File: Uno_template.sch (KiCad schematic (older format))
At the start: 4 parts

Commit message: initial commit
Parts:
- J1, J4: renamed from J?; footprint (none) -> Pin_Headers:Pin_Header_Straight_1x08_Pitch2.54mm
- J2: renamed from J?; footprint (none) -> Pin_Headers:Pin_Header_Straight_1x06_Pitch2.54mm
- J3: renamed from J?; footprint (none) -> Pin_Headers:Pin_Header_Straight_1x10_Pitch2.54mm
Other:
- note added: "Heizungssteuerung"
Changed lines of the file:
@@
 LIBS:contrib
 LIBS:valves
+LIBS:Uno_template-cache
 EELAYER 25 0
 EELAYER END
@@
 $EndDescr
 $Comp
-L Conn_01x08 J?
+L Conn_01x08 J1
 U 1 1 5A4D3F50
 P 7350 1250
-F 0 "J?" H 7350 1650 50  0000 C CNN
+F 0 "J1" H 7350 1650 50  0000 C CNN
 F 1 "POWER" H 7350 750 50  0000 C CNN
-F 2 "" H 7350 1250 50  0001 C CNN
+F 2 "Pin_Headers:Pin_Header_Straight_1x08_Pitch2.54mm" H 7350 1250 50  0001 C CNN
 F 3 "" H 7350 1250 50  0001 C CNN
 	1    7350 1250
@@
 1 = N.C.\n2 = IOREF\n3 = RESET\n4 = 3.3V\n5 = 5V\n6 = GND\n7 = GND\n8 = Vin
 $Comp
-L Conn_01x06 J?
+L Conn_01x06 J2
 U 1 1 5A4D408D
 P 7350 2350
-F 0 "J?" H 7350 2650 50  0000 C CNN
+F 0 "J2" H 7350 2650 50  0000 C CNN
 F 1 "ANALOG IN" H 7350 1950 50  0000 C CNN
-F 2 "" H 7350 2350 50  0001 C CNN
+F 2 "Pin_Headers:Pin_Header_Straight_1x06_Pitch2.54mm" H 7350 2350 50  0001 C CNN
 F 3 "" H 7350 2350 50  0001 C CNN
 	1    7350 2350
@@
 1 = A0\n2 = A1\n3 = A2\n4 = A3\n5 = A4\n6 = A5
 $Comp
-L Conn_01x08 J?
+L Conn_01x08 J4
 U 1 1 5A4D413D
 P 9850 2350
-F 0 "J?" H 9850 1850 50  0000 C CNN
+F 0 "J4" H 9850 1850 50  0000 C CNN
 F 1 "IOL" H 9850 2750 50  0000 C CNN
-F 2 "" H 9850 2350 50  0001 C CNN
+F 2 "Pin_Headers:Pin_Header_Straight_1x08_Pitch2.54mm" H 9850 2350 50  0001 C CNN
 F 3 "" H 9850 2350 50  0001 C CNN
 	1    9850 2350
@@
 $EndComp
 $Comp
-L Conn_01x10 J?
+L Conn_01x10 J3
 U 1 1 5A4D4192
 P 9850 1250
-F 0 "J?" H 9850 650 50  0000 C CNN
+F 0 "J3" H 9850 650 50  0000 C CNN
 F 1 "IOH" H 9850 1750 50  0000 C CNN
-F 2 "" H 9850 1250 50  0001 C CNN
+F 2 "Pin_Headers:Pin_Header_Straight_1x10_Pitch2.54mm" H 9850 1250 50  0001 C CNN
 F 3 "" H 9850 1250 50  0001 C CNN
 	1    9850 1250
@@
 Vin
 $Comp
-L +3V3 #PWR?
+L +3V3 #PWR01
 U 1 1 5A4D447E
 P 8300 1150
-F 0 "#PWR?" H 8300 1000 50  0001 C CNN
+F 0 "#PWR01" H 8300 1000 50  0001 C CNN
 F 1 "+3V3" H 8300 1290 50  0000 C CNN
 F 2 "" H 8300 1150 50  0001 C CNN
@@
 $EndComp
 $Comp
-L +5V #PWR?
+L +5V #PWR02
 U 1 1 5A4D449A
 P 8450 1250
-F 0 "#PWR?" H 8450 1100 50  0001 C CNN
+F 0 "#PWR02" H 8450 1100 50  0001 C CNN
 F 1 "+5V" H 8450 1390 50  0000 C CNN
 F 2 "" H 8450 1250 50  0001 C CNN
@@
 $EndComp
 $Comp
-L GND #PWR?
+L GND #PWR03
 U 1 1 5A4D44D1
 P 8300 1650
-F 0 "#PWR?" H 8300 1400 50  0001 C CNN
+F 0 "#PWR03" H 8300 1400 50  0001 C CNN
 F 1 "GND" H 8300 1500 50  0000 C CNN
 F 2 "" H 8300 1650 50  0001 C CNN
@@
 RX
 $Comp
-L GND #PWR?
+L GND #PWR04
 U 1 1 5A4D49BF
 P 8900 1150
-F 0 "#PWR?" H 8900 900 50  0001 C CNN
+F 0 "#PWR04" H 8900 900 50  0001 C CNN
 F 1 "GND" H 8900 1000 50  0000 C CNN
 F 2 "" H 8900 1150 50  0001 C CNN
@@
 Wire Wire Line
 	8900 1050 8900 1150
+Text Notes 7450 6950 0    197  ~ 0
+Heizungssteuerung
 $EndSCHEMATC

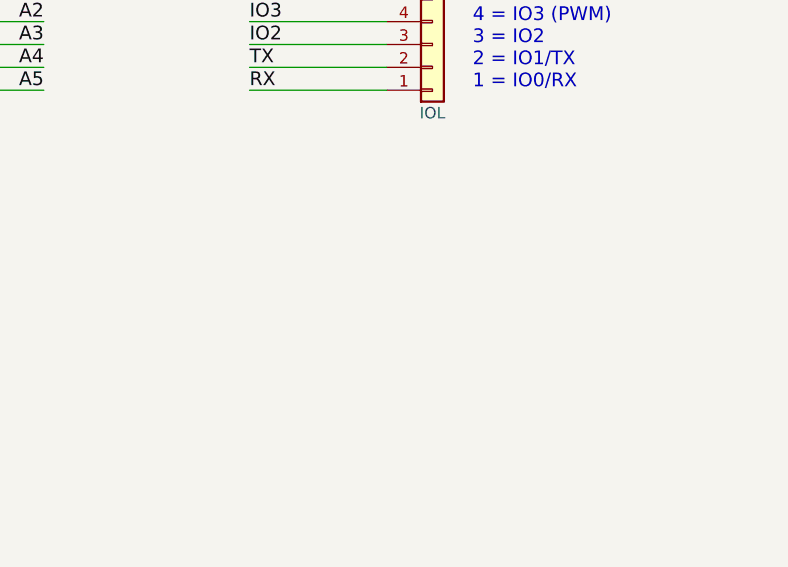
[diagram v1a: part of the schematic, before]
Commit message: Schaltplan: 1Wire interface added
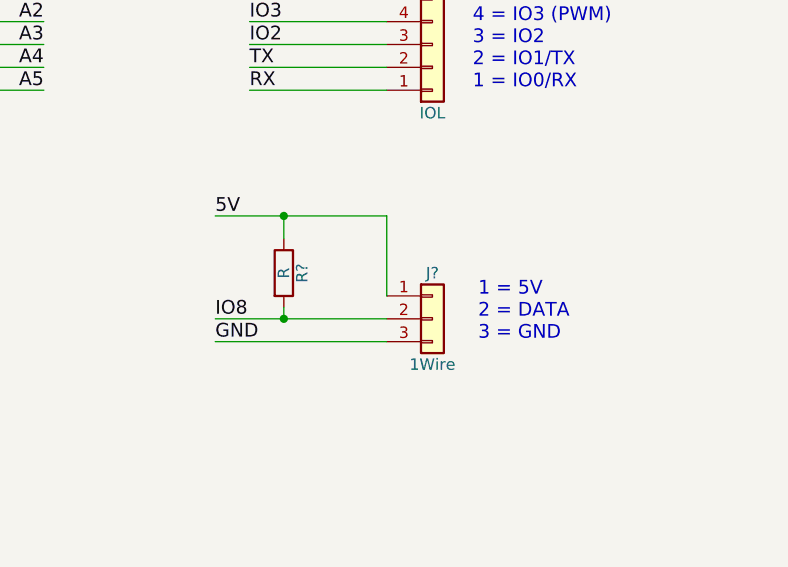
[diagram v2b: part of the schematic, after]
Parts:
- added J?: 1Wire, symbol Conn_01x03
- added R?: R, symbol R
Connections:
- net +5V: now also J?.1 (Pin_1), R?.1
- net GND: now also J?.3 (Pin_3)
- net IO8: now also J?.2 (Pin_2), R?.2
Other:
- note added: "1 = 5V\n2 = DATA\n3 = GND"
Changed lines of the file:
@@
 	1    0    0    -1
 $EndComp
-Wire Wire Line
-	7550 1050 8150 1050
-Wire Wire Line
-	7550 1150 8150 1150
-Wire Wire Line
-	7550 1250 8300 1250
-Wire Wire Line
-	7550 1350 8450 1350
-Wire Wire Line
-	7550 1450 8300 1450
-Wire Wire Line
-	7550 1550 8300 1550
-Wire Wire Line
-	7550 1650 8150 1650
-Wire Wire Line
-	8300 1250 8300 1150
-Wire Wire Line
-	8450 1350 8450 1250
-Wire Wire Line
-	8300 1450 8300 1650
-Connection ~ 8300 1550
-Wire Wire Line
-	7550 2150 8150 2150
-Wire Wire Line
-	7550 2250 8150 2250
-Wire Wire Line
-	7550 2350 8150 2350
-Wire Wire Line
-	7550 2450 8150 2450
-Wire Wire Line
-	7550 2550 8150 2550
-Wire Wire Line
-	7550 2650 8150 2650
 Text Label 8150 2150 2    60   ~ 0
 A0
@@
 Text Label 8150 2650 2    60   ~ 0
 A5
-Wire Wire Line
-	9050 1550 9650 1550
-Wire Wire Line
-	9650 1650 9050 1650
-Wire Wire Line
-	9650 1450 9050 1450
-Wire Wire Line
-	9650 1350 9050 1350
-Wire Wire Line
-	9650 1250 9050 1250
-Wire Wire Line
-	9650 1150 9050 1150
-Wire Wire Line
-	8900 1050 9650 1050
-Wire Wire Line
-	9650 950  9050 950
-Wire Wire Line
-	9650 850  9050 850
-Wire Wire Line
-	9650 750  9050 750
-Wire Wire Line
-	9650 1950 9050 1950
-Wire Wire Line
-	9650 2050 9050 2050
-Wire Wire Line
-	9650 2150 9050 2150
-Wire Wire Line
-	9650 2250 9050 2250
-Wire Wire Line
-	9650 2350 9050 2350
-Wire Wire Line
-	9650 2450 9050 2450
-Wire Wire Line
-	9650 2550 9050 2550
-Wire Wire Line
-	9650 2650 9050 2650
 Text Label 9050 750  0    60   ~ 0
 A5
@@
 	1    0    0    -1
 $EndComp
+Text Notes 7450 6950 0    197  ~ 0
+Heizungssteuerung
+$Comp
+L Conn_01x03 J?
+U 1 1 5A4DF07A
+P 9850 3650
+F 0 "J?" H 9850 3850 50  0000 C CNN
+F 1 "1Wire" H 9850 3450 50  0000 C CNN
+F 2 "" H 9850 3650 50  0001 C CNN
+F 3 "" H 9850 3650 50  0001 C CNN
+	1    9850 3650
+	1    0    0    -1
+$EndComp
+$Comp
+L R R?
+U 1 1 5A4DF0E4
+P 9200 3450
+F 0 "R?" V 9280 3450 50  0000 C CNN
+F 1 "R" V 9200 3450 50  0000 C CNN
+F 2 "" V 9130 3450 50  0001 C CNN
+F 3 "" H 9200 3450 50  0001 C CNN
+	1    9200 3450
+	1    0    0    -1
+$EndComp
+Text Label 8900 3750 0    60   ~ 0
+GND
+Text Label 8900 3650 0    60   ~ 0
+IO8
+Text Label 8900 3200 0    60   ~ 0
+5V
+Wire Wire Line
+	7550 1050 8150 1050
+Wire Wire Line
+	7550 1150 8150 1150
+Wire Wire Line
+	7550 1250 8300 1250
+Wire Wire Line
+	7550 1350 8450 1350
+Wire Wire Line
+	7550 1450 8300 1450
+Wire Wire Line
+	7550 1550 8300 1550
+Wire Wire Line
+	7550 1650 8150 1650
+Wire Wire Line
+	8300 1250 8300 1150
+Wire Wire Line
+	8450 1350 8450 1250
+Wire Wire Line
+	8300 1450 8300 1650
+Connection ~ 8300 1550
+Wire Wire Line
+	7550 2150 8150 2150
+Wire Wire Line
+	7550 2250 8150 2250
+Wire Wire Line
+	7550 2350 8150 2350
+Wire Wire Line
+	7550 2450 8150 2450
+Wire Wire Line
+	7550 2550 8150 2550
+Wire Wire Line
+	7550 2650 8150 2650
+Wire Wire Line
+	9050 1550 9650 1550
+Wire Wire Line
+	9650 1650 9050 1650
+Wire Wire Line
+	9650 1450 9050 1450
+Wire Wire Line
+	9650 1350 9050 1350
+Wire Wire Line
+	9650 1250 9050 1250
+Wire Wire Line
+	9650 1150 9050 1150
+Wire Wire Line
+	8900 1050 9650 1050
+Wire Wire Line
+	9650 950  9050 950
+Wire Wire Line
+	9650 850  9050 850
+Wire Wire Line
+	9650 750  9050 750
+Wire Wire Line
+	9650 1950 9050 1950
+Wire Wire Line
+	9650 2050 9050 2050
+Wire Wire Line
+	9650 2150 9050 2150
+Wire Wire Line
+	9650 2250 9050 2250
+Wire Wire Line
+	9650 2350 9050 2350
+Wire Wire Line
+	9650 2450 9050 2450
+Wire Wire Line
+	9650 2550 9050 2550
+Wire Wire Line
+	9650 2650 9050 2650
 Wire Wire Line
 	8900 1050 8900 1150
-Text Notes 7450 6950 0    197  ~ 0
-Heizungssteuerung
+Wire Wire Line
+	8900 3200 9650 3200
+Wire Wire Line
+	9200 3200 9200 3300
+Wire Wire Line
+	9200 3600 9200 3650
+Wire Wire Line
+	8900 3650 9650 3650
+Wire Wire Line
+	9650 3200 9650 3550
+Connection ~ 9200 3200
+Connection ~ 9200 3650
+Wire Wire Line
+	9650 3750 8900 3750
+Text Notes 10050 3750 0    60   ~ 0
+1 = 5V\n2 = DATA\n3 = GND
 $EndSCHEMATC
